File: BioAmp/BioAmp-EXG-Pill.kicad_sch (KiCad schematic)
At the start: 44 parts, among them IC3 MAX1169BEUD+, J1 Conn_01x03_Pin, J2 Conn_01x04_Pin, J3 Conn_01x04_Pin, U1 TL074HIPWR

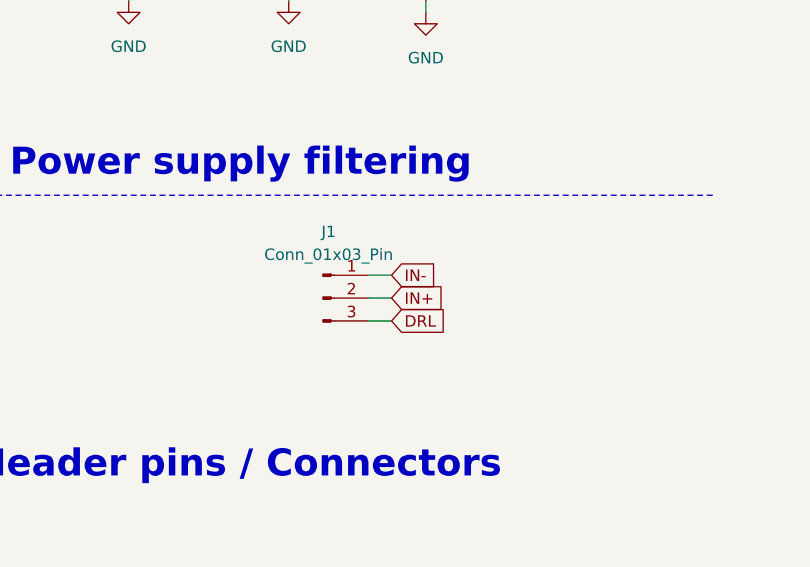
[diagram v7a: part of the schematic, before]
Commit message: Exposed J1 4th pin to add a do-not-connect
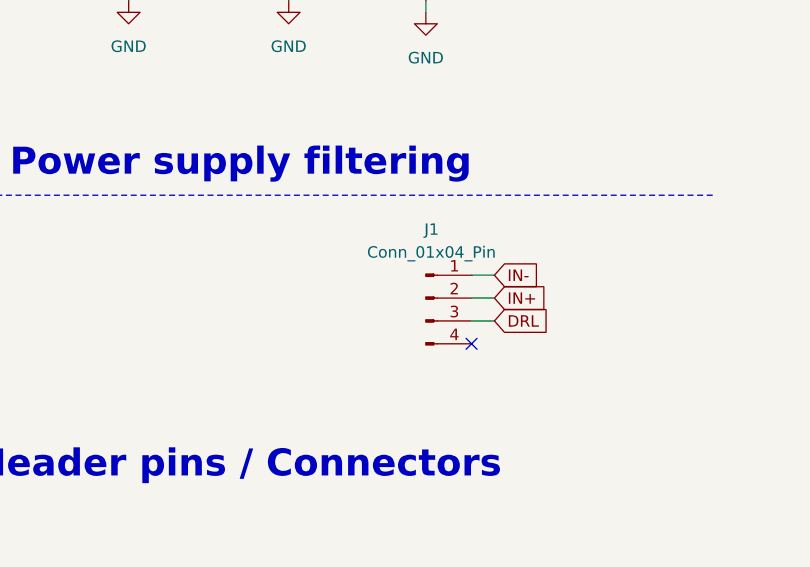
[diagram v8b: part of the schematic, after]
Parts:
- removed J1: Conn_01x03_Pin, Connector_FFC-FPC:Molex_200528-0040_1x04-1MP_P1.00mm_Horizontal, symbol Connector:Conn_01x03_Pin
- added J1: Conn_01x04_Pin, Connector_FFC-FPC:Molex_200528-0040_1x04-1MP_P1.00mm_Horizontal, symbol Connector:Conn_01x04_Pin
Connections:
- net DRL: now also J1.3 (Pin_3)
- net IN+: now also J1.2 (Pin_2)
- net IN-: now also J1.1 (Pin_1)
- no-connect marks 0 -> 1
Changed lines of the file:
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@@
 		(color 0 0 0 0)
 	)
+	(no_connect
+		(at 257.81 149.86)
+	)
 	(wire
 		(pts
@@
 	(wire
 		(pts
-			(xy 246.38 144.78) (xy 248.92 144.78)
+			(xy 257.81 144.78) (xy 260.35 144.78)
 		)
 		(stroke
@@
 	(wire
 		(pts
-			(xy 246.38 147.32) (xy 248.92 147.32)
+			(xy 257.81 147.32) (xy 260.35 147.32)
 		)
 		(stroke
@@
 	(wire
 		(pts
-			(xy 246.38 142.24) (xy 248.92 142.24)
+			(xy 257.81 142.24) (xy 260.35 142.24)
 		)
 		(stroke
@@
 	(global_label "DRL"
 		(shape input)
-		(at 248.92 147.32 0)
+		(at 260.35 147.32 0)
 		(fields_autoplaced yes)
 		(effects
@@
 		)
 		(property "Intersheetrefs" "${INTERSHEET_REFS}"
-			(at 254.8191 147.32 0)
+			(at 266.2491 147.32 0)
 			(hide yes)
 			(show_name no)
@@
 	(global_label "IN+"
 		(shape input)
-		(at 248.92 144.78 0)
+		(at 260.35 144.78 0)
 		(fields_autoplaced yes)
 		(effects
@@
 		)
 		(property "Intersheetrefs" "${INTERSHEET_REFS}"
-			(at 254.7587 144.78 0)
+			(at 266.1887 144.78 0)
 			(hide yes)
 			(show_name no)
@@
 	(global_label "IN-"
 		(shape input)
-		(at 248.92 142.24 0)
+		(at 260.35 142.24 0)
 		(fields_autoplaced yes)
 		(effects
@@
 		)
 		(property "Intersheetrefs" "${INTERSHEET_REFS}"
-			(at 254.7587 142.24 0)
+			(at 266.1887 142.24 0)
 			(hide yes)
 			(show_name no)
@@
 	)
 	(symbol
+		(lib_id "Connector:Conn_01x04_Pin")
+		(at 252.73 144.78 0)
+		(unit 1)
+		(body_style 1)
+		(exclude_from_sim no)
+		(in_bom yes)
+		(on_board yes)
+		(in_pos_files yes)
+		(dnp no)
+		(fields_autoplaced yes)
+		(property "Reference" "J1"
+			(at 253.365 137.16 0)
+			(show_name no)
+			(do_not_autoplace no)
+			(effects
+				(font
+					(size 1.27 1.27)
+				)
+			)
+		)
+		(property "Value" "Conn_01x04_Pin"
+			(at 253.365 139.7 0)
+			(show_name no)
+			(do_not_autoplace no)
+			(effects
+				(font
+					(size 1.27 1.27)
+				)
+			)
+		)
+		(property "Footprint" "Connector_FFC-FPC:Molex_200528-0040_1x04-1MP_P1.00mm_Horizontal"
+			(at 252.73 144.78 0)
+			(hide yes)
+			(show_name no)
+			(do_not_autoplace no)
+			(effects
+				(font
+					(size 1.27 1.27)
+				)
+			)
+		)
+		(property "Datasheet" ""
+			(at 252.73 144.78 0)
+			(hide yes)
+			(show_name no)
+			(do_not_autoplace no)
+			(effects
+				(font
+					(size 1.27 1.27)
+				)
+			)
+		)
+		(property "Description" "Generic connector, single row, 01x04, script generated"
+			(at 252.73 144.78 0)
+			(hide yes)
+			(show_name no)
+			(do_not_autoplace no)
+			(effects
+				(font
+					(size 1.27 1.27)
+				)
+			)
+		)
+		(pin "4"
+		)
+		(pin "2"
+		)
+		(pin "3"
+		)
+		(pin "1"
+		)
+		(instances
+			(project "BioAmp-EXG-Pill"
+				(path "/6820f13c-3971-4615-b87b-c2f927031906"
+					(reference "J1")
+					(unit 1)
+				)
+			)
+		)
+	)
+	(symbol
 		(lib_id "Device:D_Zener")
 		(at 114.3 167.64 270)
@@
 					(unit 1)
 				)
-			)
-		)
-	)
-	(symbol
-		(lib_id "Connector:Conn_01x03_Pin")
-		(at 241.3 144.78 0)
-		(unit 1)
-		(body_style 1)
-		(exclude_from_sim no)
-		(in_bom yes)
-		(on_board yes)
-		(in_pos_files yes)
-		(dnp no)
-		(fields_autoplaced yes)
-		(property "Reference" "J1"
-			(at 241.935 137.414 0)
-			(show_name no)
-			(do_not_autoplace no)
-			(effects
-				(font
-					(size 1.27 1.27)
-				)
-			)
-		)
-		(property "Value" "Conn_01x03_Pin"
-			(at 241.935 139.954 0)
-			(show_name no)
-			(do_not_autoplace no)
-			(effects
-				(font
-					(size 1.27 1.27)
-				)
-			)
-		)
-		(property "Footprint" "Connector_FFC-FPC:Molex_200528-0040_1x04-1MP_P1.00mm_Horizontal"
-			(at 241.3 144.78 0)
-			(hide yes)
-			(show_name no)
-			(do_not_autoplace no)
-			(effects
-				(font
-					(size 1.27 1.27)
-				)
-			)
-		)
-		(property "Datasheet" ""
-			(at 241.3 144.78 0)
-			(hide yes)
-			(show_name no)
-			(do_not_autoplace no)
-			(effects
-				(font
-					(size 1.27 1.27)
-				)
-			)
-		)
-		(property "Description" "Generic connector, single row, 01x03, script generated"
-			(at 241.3 144.78 0)
-			(hide yes)
-			(show_name no)
-			(do_not_autoplace no)
-			(effects
-				(font
-					(size 1.27 1.27)
-				)
-			)
-		)
-		(pin "1"
-		)
-		(pin "3"
-		)
-		(pin "2"
-		)
-		(instances
-			(project "BioAmp-EXG-Pill"
-				(path "/6820f13c-3971-4615-b87b-c2f927031906"
-					(reference "J1")
-					(unit 1)
-				)
